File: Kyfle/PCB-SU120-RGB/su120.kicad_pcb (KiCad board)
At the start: 2 copper layers, 96.2 x 95.9 mm, 160 parts, among them J1 MJ-4PP-9, J2 Conn_01x03, J3 Conn_01x08, J4 Conn_01x08, J6 MJ-4PP-9, SW1 SW_PUSH_LED, SW10 SW_PUSH_LED, SW11 SW_PUSH_LED, SW12 SW_PUSH_LED, SW13 SW_PUSH_LED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

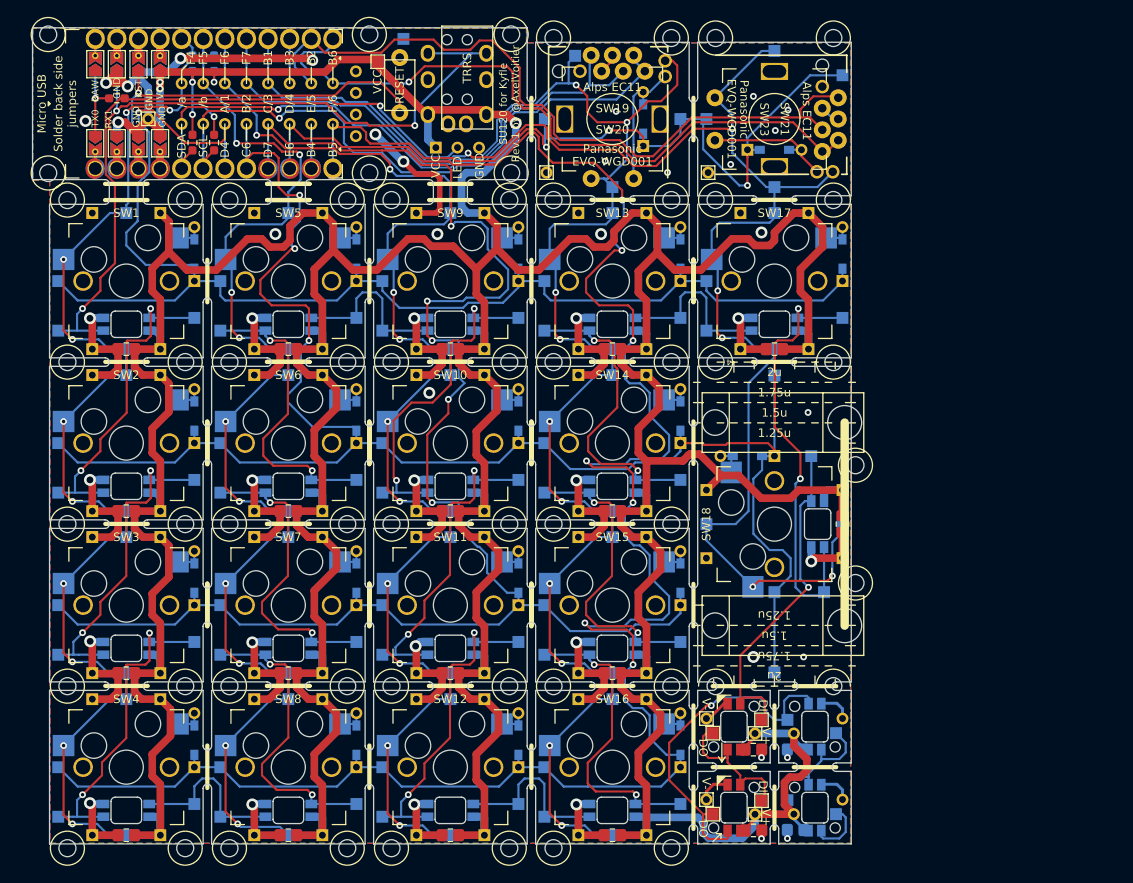
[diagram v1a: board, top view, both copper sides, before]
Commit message: It's never done, part 2. Making all col/row/led signals accessible on front side
The had been previously removed to reduce number of drill impacts.
But if we have access to the these signals also from the front, we can wire the boards from the switch side as well.
Provide more flexibility, notably when not using any top plate.
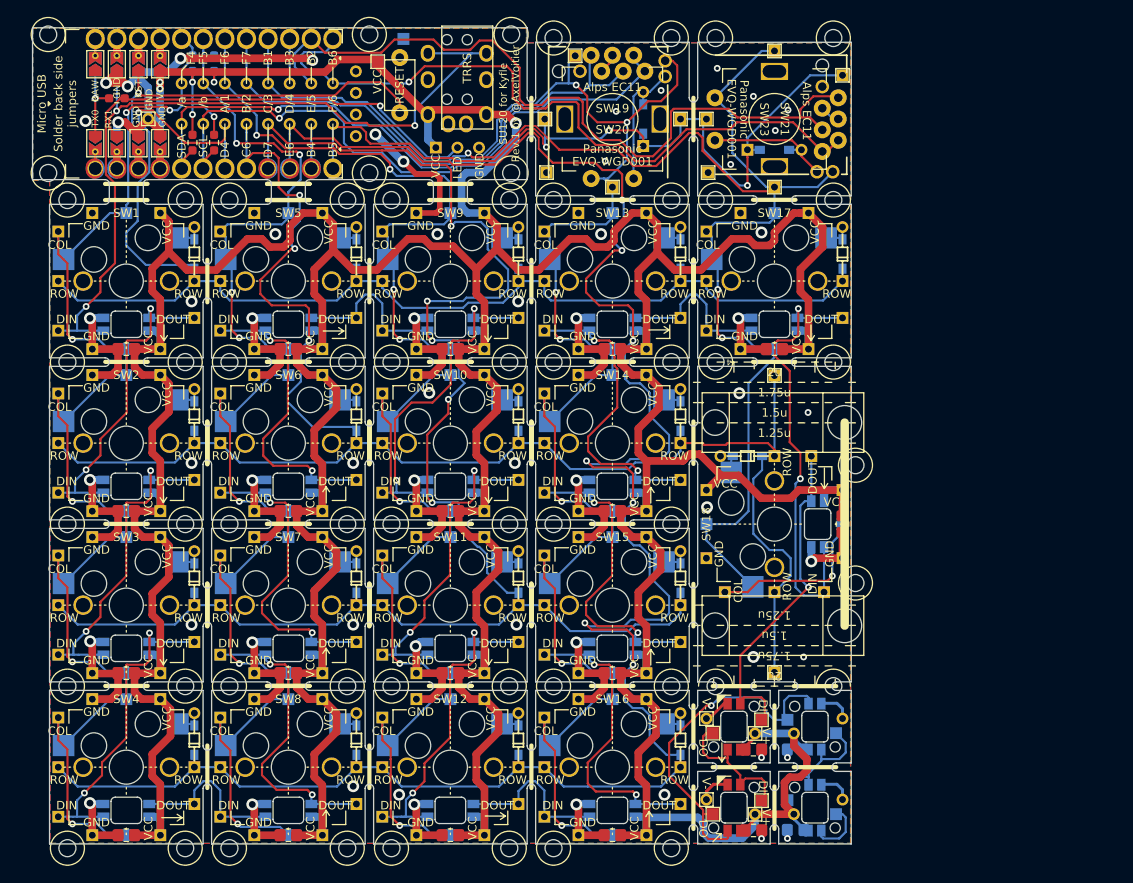
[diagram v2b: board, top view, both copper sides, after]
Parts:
- H133, H134, H135, H136, H137, H138, H139, H140, H46, H50: footprint Kyfle Footprints:1pad_conn -> Kyfle Footprints:1pin_rect_conn
- H170, H171: footprint Kyfle Footprints:1pin_conn -> Kyfle Footprints:1pin_rect_conn
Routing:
- net X1: track 142.3 -> 170.7 mm, vias 10 -> 6
- net X2: track 145.2 -> 167.8 mm, vias 10 -> 7
- net X3: track 157.7 -> 180.0 mm, vias 10 -> 7
- net X4: track 207.2 -> 229.2 mm, vias 10 -> 7
- net X5: track 184.7 -> 200.6 mm, vias 6 -> 4
- net X7: track 87.0 -> 90.7 mm
- net Net-(SW12-Pad2): track 20.4 -> 19.2 mm
- net Net-(SW13-Pad2): track 20.5 -> 19.3 mm
- net Y4: track 250.7 -> 251.8 mm
- net X8: track 82.2 -> 83.3 mm
- net Net-(SW5-Pad2): track 20.3 -> 19.4 mm
- net Net-(SW4-Pad2): track 20.1 -> 19.3 mm
- net Y1: track 158.9 -> 158.3 mm
- net GND: vias 45 -> 59

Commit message: PCB: It's never done, part 3
- Rotated 90 degrees the lonely 1u at top right to give some more design 
options to user.
- Made a special footprint for switch module that are used in rotated 
conditions (that new rotated 1u, and also the 2u one).
- Updated fab for roller encoder to show direction of the roll.
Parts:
- added ?: , Kyfle Footprints:M2_Hole_Standoff_Large_Cleareance, F.Cu at (134.7, 95.2)
- added ?: , Kyfle Footprints:M2_Hole_Standoff_Large_Cleareance, F.Cu at (120.9, 95.2)
- SW17, SW18: footprint Kyfle Footprints:CherryMX_Kyfle_v1_Module -> Kyfle Footprints:CherryMX_Kyfle_v1_Module_For_Rotated
- turned SW17 to 270 degrees
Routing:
- net X5: track 200.6 -> 216.7 mm
- net VCC: track 744.0 -> 729.0 mm
- net Net-(SW17-Pad2): track 52.0 -> 60.0 mm, vias 2 -> 1
- net Y1: track 158.3 -> 165.2 mm, vias 1 -> 2
- net Net-(H154-Pad1): track 39.6 -> 45.1 mm
- net Y2: track 199.2 -> 203.3 mm
- net Net-(SW13-Pad2): track 19.3 -> 22.7 mm
- net GND: vias 59 -> 58
- net (no net): vias 0 -> 1

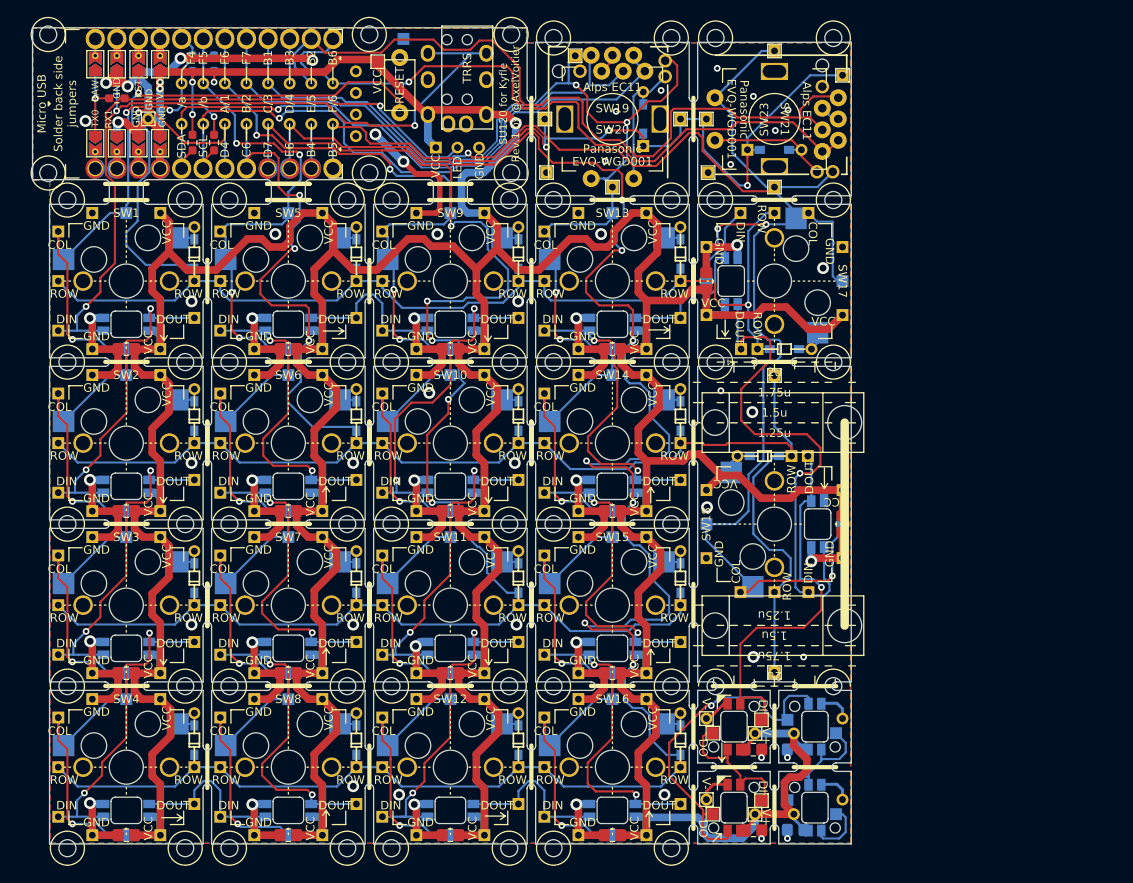
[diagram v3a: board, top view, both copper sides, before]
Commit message: It's never... well, at this point it is almost a v17 :D
- Decided to put the M2 mounting holes on all sides, and not just top-bottom.
They won't be used in most case (unless I actually figure out they could help in the thumb cluster/row).
But it allows to freely orient them sideways (ie. 90 deg left or right) for even more flexibility.

The one switch (top right corner) as well as the encoder bit board that was previously turned 90 degrees will be redone in a future commit once I decide how to integrate the 5-way switch.

- I made all the holes of the MX switch and their hotswap socket as plated for ground continuation.
Not only it will mechanically improve them. It will also help with general grounding and in most cases prevent additional ground vias.
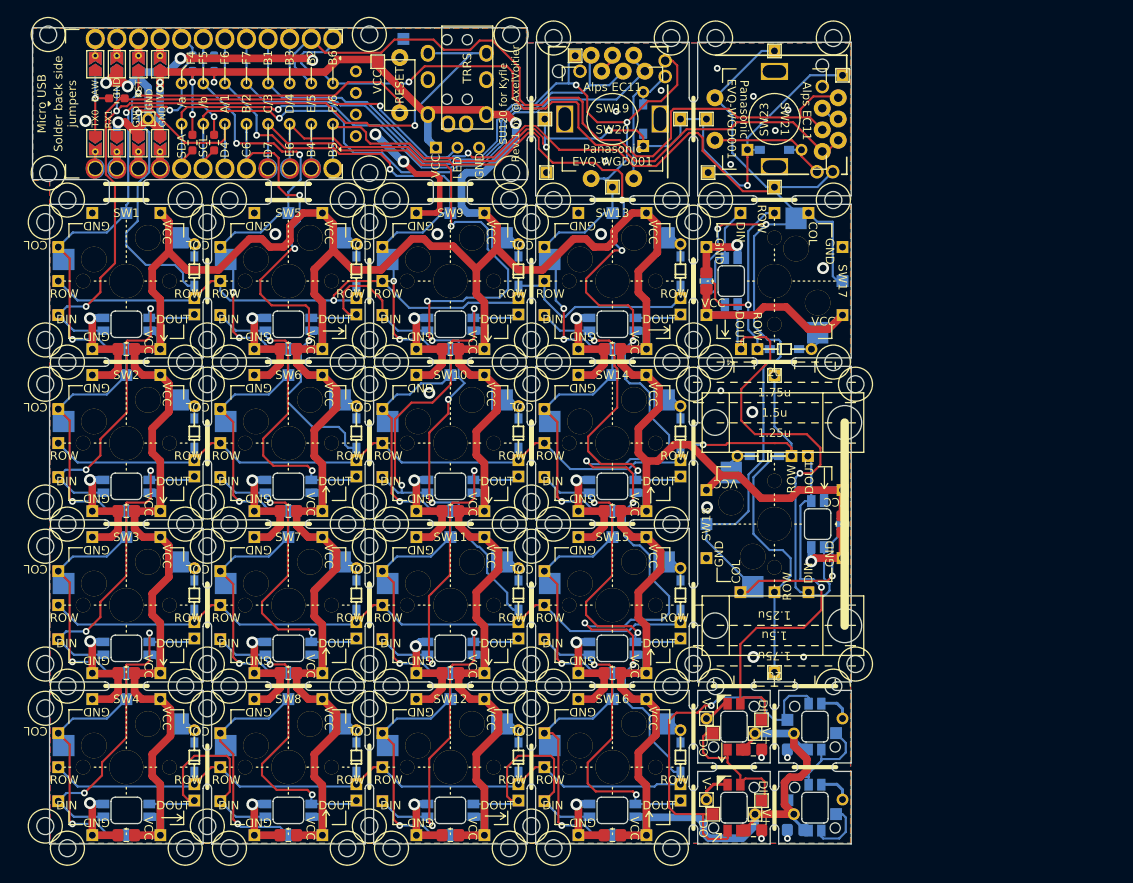
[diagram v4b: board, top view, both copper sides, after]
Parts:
- added ?: , Kyfle Footprints:M2_Hole_Standoff_Large_Cleareance, F.Cu at (137.3, 97.9)
- added ?: , Kyfle Footprints:M2_Hole_Standoff_Large_Cleareance, F.Cu at (137.3, 130.7)
- added ?: , Kyfle Footprints:M2_Hole_Standoff_Large_Cleareance, F.Cu at (118.3, 130.7)
- added ?: , Kyfle Footprints:M2_Hole_Standoff_Large_Cleareance, F.Cu at (118.3, 97.9)
- added ?: , Kyfle Footprints:M2_Hole_Standoff_Large_Cleareance, F.Cu at (118.3, 92.6)
- added ?: , Kyfle Footprints:M2_Hole_Standoff_Large_Cleareance, F.Cu at (118.3, 78.8)
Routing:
- net X1: track 170.7 -> 156.2 mm
- net X3: track 180.0 -> 167.6 mm
- net X2: track 167.8 -> 155.4 mm
- net X4: track 229.2 -> 217.1 mm
- net Net-(SW12-Pad2): track 19.2 -> 28.2 mm
- net Net-(SW4-Pad2): track 19.3 -> 28.0 mm
- net VCC: track 729.0 -> 722.3 mm
- net Net-(SW13-Pad2): track 22.7 -> 16.6 mm
- net Net-(H157-Pad1): track 41.5 -> 44.9 mm
- net Net-(SW5-Pad2): track 19.4 -> 22.6 mm
- net Net-(SW10-Pad2): track 38.4 -> 40.2 mm
- net Net-(SW11-Pad2): track 38.4 -> 40.2 mm
- net Net-(SW1-Pad2): track 38.4 -> 39.7 mm
- net Net-(SW3-Pad2): track 38.1 -> 39.3 mm
- net Net-(SW2-Pad2): track 38.5 -> 39.7 mm
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
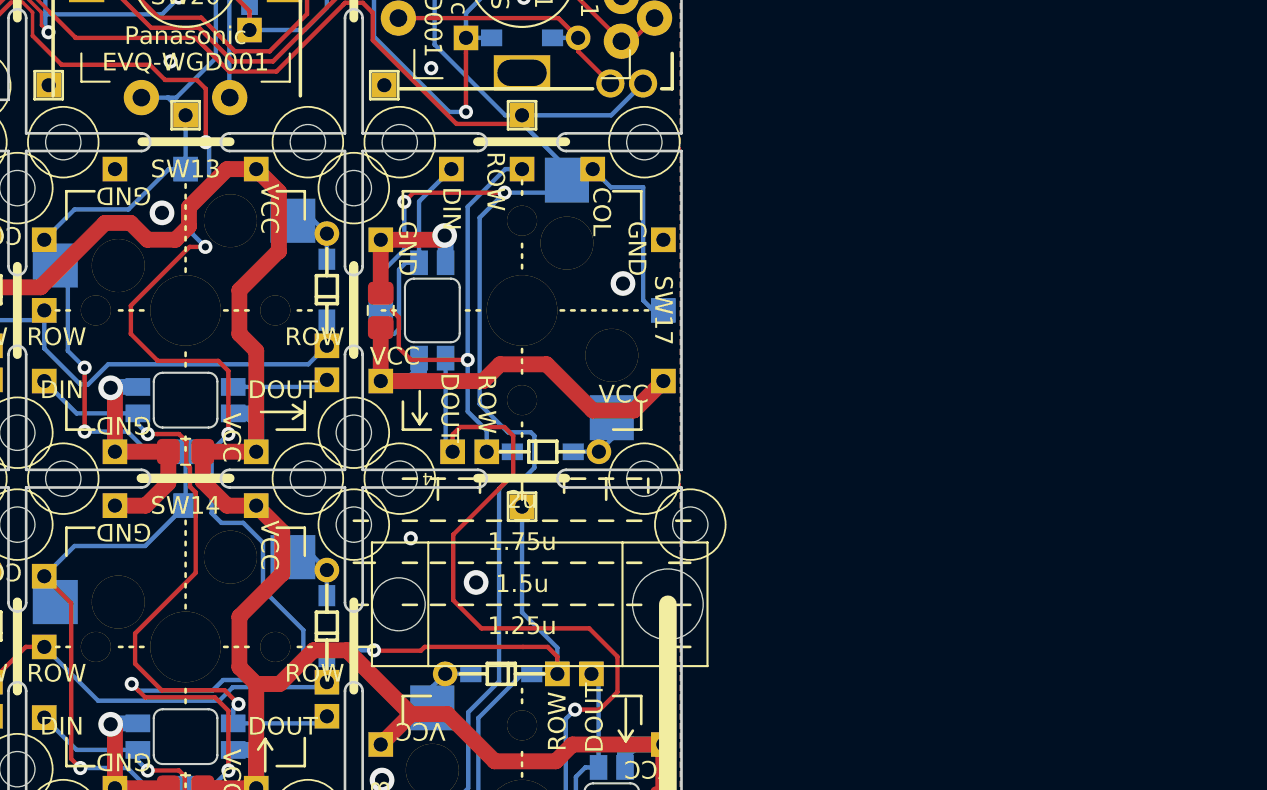
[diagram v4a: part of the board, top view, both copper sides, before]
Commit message: Tentative routing of the 5-way switch
Not yet integrated in the main board itself.
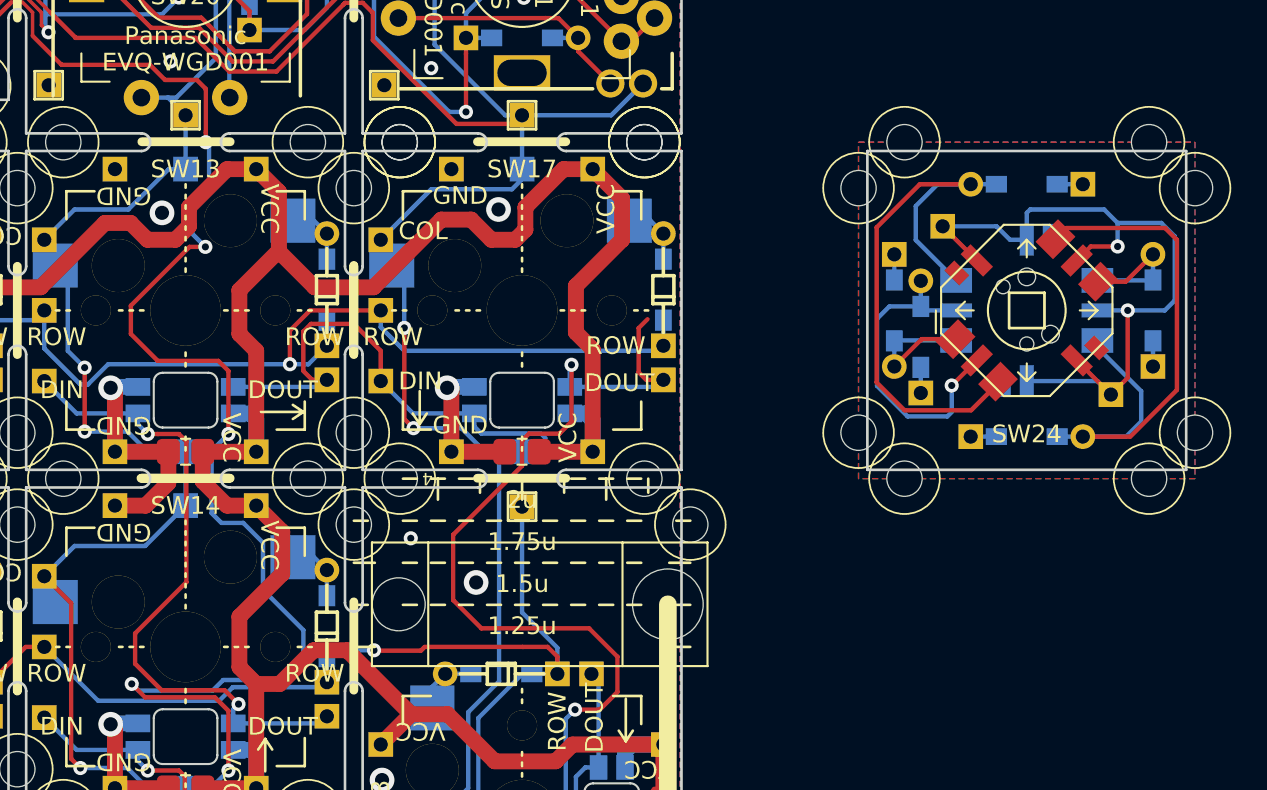
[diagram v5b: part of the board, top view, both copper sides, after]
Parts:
- removed the ? at (96.6, 76.2)
- removed the ? at (82.8, 76.2)
- removed the ? at (77.6, 76.2)
- removed the ? at (63.7, 76.2)
- removed the ? at (58.5, 76.2)
- removed the ? at (44.7, 76.2)
- removed the ? at (101.8, 57.1)
- removed the ? at (115.7, 57.1)
- removed the ? at (120.9, 57.1)
- removed the ? at (134.7, 57.1)
- removed the ? at (134.7, 76.2)
- removed the ? at (120.9, 76.2)
- removed the ? at (101.8, 76.2)
- removed the ? at (115.7, 76.2)
- removed the ? at (118.3, 92.6)
- removed the ? at (118.3, 78.8)
- removed the ? at (134.7, 95.2)
- removed the ? at (120.9, 95.2)
- added %R: SW_Push, Kyfle Footprints:CherryMX_Kyfle_v1_Module_2_M2, F.Cu at (51.6, 85.7)
- added %R: SW_Push, Kyfle Footprints:CherryMX_Kyfle_v1_Module_2_M2, F.Cu at (127.8, 66.7)
- added %R (x4): SW_Push, Kyfle Footprints:CherryMX_Kyfle_v1_Module_2_M2, F.Cu at (127.8, 85.7)
- added %R: SW_Push, Kyfle Footprints:CherryMX_Kyfle_v1_Module_2_M2, F.Cu at (70.6, 85.7)
- added %R: SW_Push, Kyfle Footprints:CherryMX_Kyfle_v1_Module_2_M2, F.Cu at (89.7, 85.7)
- added %R (x4): SW_Push, Kyfle Footprints:CherryMX_Kyfle_v1_Module_2_M2, F.Cu at (156.4, 85.7)
- added %R (x2): SW_Push, Kyfle Footprints:CherryMX_Kyfle_v1_Module_2_M2, F.Cu at (108.7, 66.7)
- added D1: D_Small, Kyfle Footprints:diode_TH_SMD_rev3, F.Cu at (148.9, 85.7)
- added D2: D_Small, Kyfle Footprints:diode_TH_SMD_rev3, F.Cu at (150.4, 87.2)
- added D3: D_Small, Kyfle Footprints:diode_TH_SMD_rev3, F.Cu at (156.4, 78.6)
- added D4: D_Small, Kyfle Footprints:diode_TH_SMD_rev3, F.Cu at (156.4, 92.9)
- added D5: D_Small, Kyfle Footprints:diode_TH_SMD_rev3, F.Cu at (163.5, 85.7)
- added H6: MountingHole_Pad, Kyfle Footprints:1pin_rect_conn, F.Cu at (151.6, 81.0)
- added H6: MountingHole_Pad, Kyfle Footprints:1pin_rect_conn, F.Cu at (161.1, 90.5)
- added SW24: 5way_switch, Kyfle Footprints:Five_Way_Switch_Panasonic_EVQQ7, B.Cu at (156.4, 85.7)
- added SW24: 5way_switch, Kyfle Footprints:Five_Way_Switch_Panasonic_EVQQ7, F.Cu at (156.4, 85.7)
- turned SW17 to 0 degrees
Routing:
- net Net-(D3-Pad2): track 0.00 -> 33.6 mm
- net Net-(D4-Pad2): track 0.00 -> 33.1 mm
- net X5: track 216.7 -> 240.1 mm, vias 4 -> 6
- net VCC: track 722.3 -> 745.3 mm
- net Net-(D2-Pad2): track 0.00 -> 18.7 mm, vias 0 -> 1
- net Net-(SW13-Pad2): track 16.6 -> 27.3 mm
- net Net-(D1-Pad2): track 0.00 -> 9.07 mm
- net Net-(D5-Pad2): track 0.00 -> 8.36 mm
- net Net-(SW17-Pad2): track 60.0 -> 67.7 mm, vias 1 -> 2
- net Y1: track 165.6 -> 167.5 mm
- net Y3: track 193.0 -> 194.4 mm
- net Y6: track 95.3 -> 96.7 mm
- net Y4: track 252.4 -> 253.9 mm
- net Y2: track 203.5 -> 205.0 mm
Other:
- board size 96.2 x 95.9 mm -> 124.8 x 95.9 mm
